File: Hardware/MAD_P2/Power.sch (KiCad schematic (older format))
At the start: 71 parts, among them J1 Line_3, J2 Line_1, J3 Line_2, J4 Power_In, U10 AMS1117-3.3, U11 APM4953, U12 APM4953, U19 AMS1117-1.8, U2 XL1509-5.0, U20 LM321, U21 APM4953, U3 XL1509-5.0, U4 XL1509-5.0, U5 XL1509-5.0, U6 AMS1117-3.3, U7 AMS1117-3.3, U8 AMS1117-3.3, U9 AMS1117-3.3

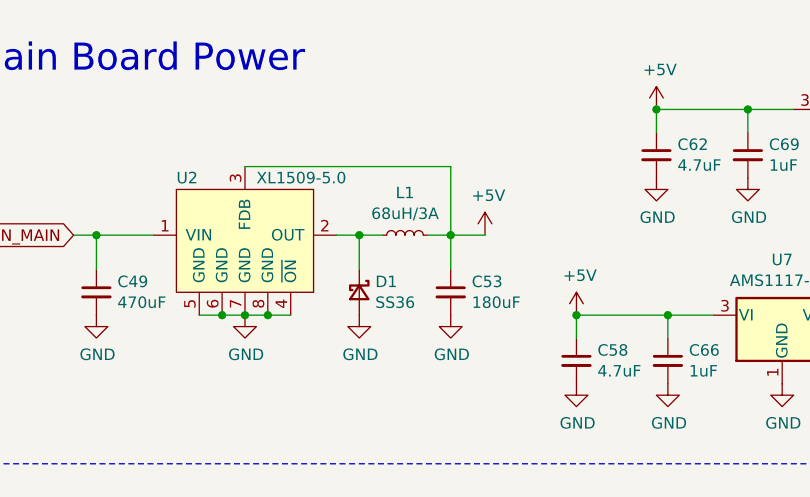
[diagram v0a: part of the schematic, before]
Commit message: added lcsc part numbers to bom
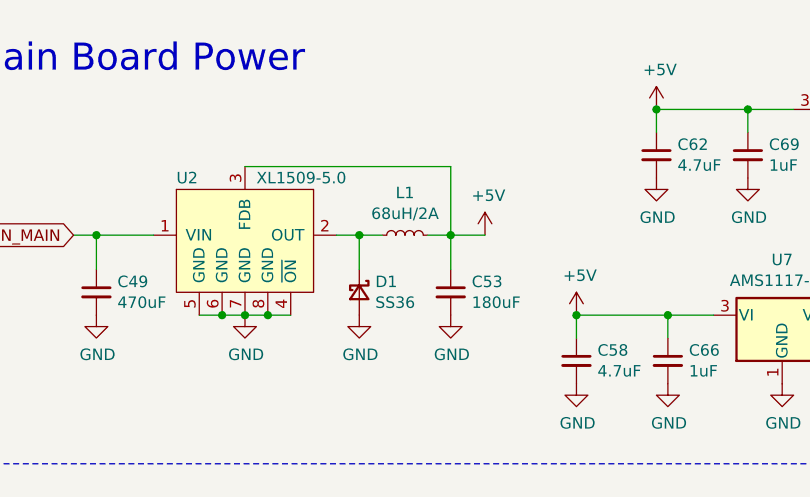
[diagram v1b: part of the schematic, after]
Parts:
- C140, C141, C142, C57, C58, C59, C60, C62, C71, C88: LCSC (none) -> C19666; TYPE (none) -> BASIC
- C49, C50, C51, C52: LCSC (none) -> C3350; TYPE (none) -> EXT
- C53, C54, C55, C56: LCSC (none) -> C413657; TYPE (none) -> EXT
- C61, C63, C64, C65, C66, C67, C68, C69, C70, C72, C89: LCSC (none) -> C15849; TYPE (none) -> BASIC
- C73, C74, C75, C91: footprint Capacitor_SMD:C_0603_1608Metric -> Capacitor_SMD:C_0805_2012Metric; LCSC (none) -> C15850; TYPE (none) -> EXT
- C90: LCSC (none) -> C14663; TYPE (none) -> BASIC
- D1, D2, D3, D4: LCSC (none) -> C35722; TYPE (none) -> BASIC
- J1, J2, J3, J4: LCSC (none) -> C431092; TYPE (none) -> EXT
- JP1, JP2, JP3, JP4, JP5, JP6, JP7, JP8, JP9: TYPE (none) -> NA
- L1: value 68uH/3A -> 68uH/2A; LCSC (none) -> C497902; TYPE (none) -> EXT
- L2, L3, L4: LCSC (none) -> C497902; TYPE (none) -> EXT
- R6, R9: LCSC (none) -> C25804; TYPE (none) -> BASIC
- U10, U6, U7, U8, U9: LCSC (none) -> C6186; TYPE (none) -> BASIC
- U11, U12, U21: LCSC (none) -> C20897; TYPE (none) -> BASIC
- U19: LCSC (none) -> C6185; TYPE (none) -> EXT
- U2, U3, U4, U5: LCSC (none) -> C61063; TYPE (none) -> BASIC
- U20: LCSC (none) -> C100068; TYPE (none) -> EXT
